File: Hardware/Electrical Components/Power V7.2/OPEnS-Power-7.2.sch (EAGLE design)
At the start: 26 parts, among them U2 DS3231SNT&R, U3 LM2575SX-5.0/NOPB

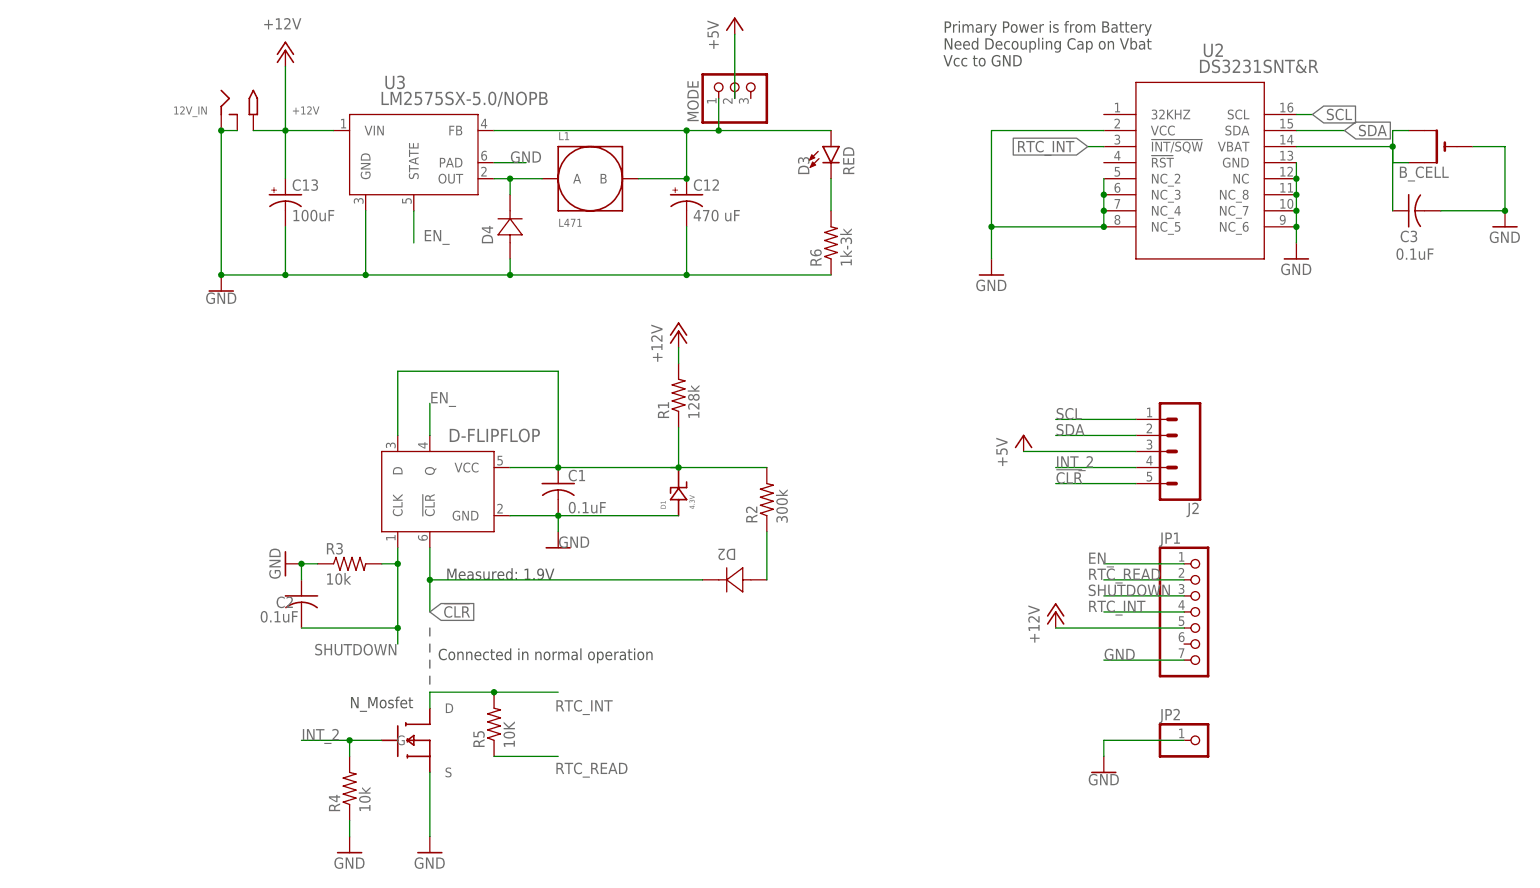
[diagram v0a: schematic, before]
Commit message: Bug fix for Powerboard 7.2V
Changed R5 and R2 value to protect against RTC_READ floating when feather is as sleep.
Added C4 capacitor to further protect against floating RTC_READ.
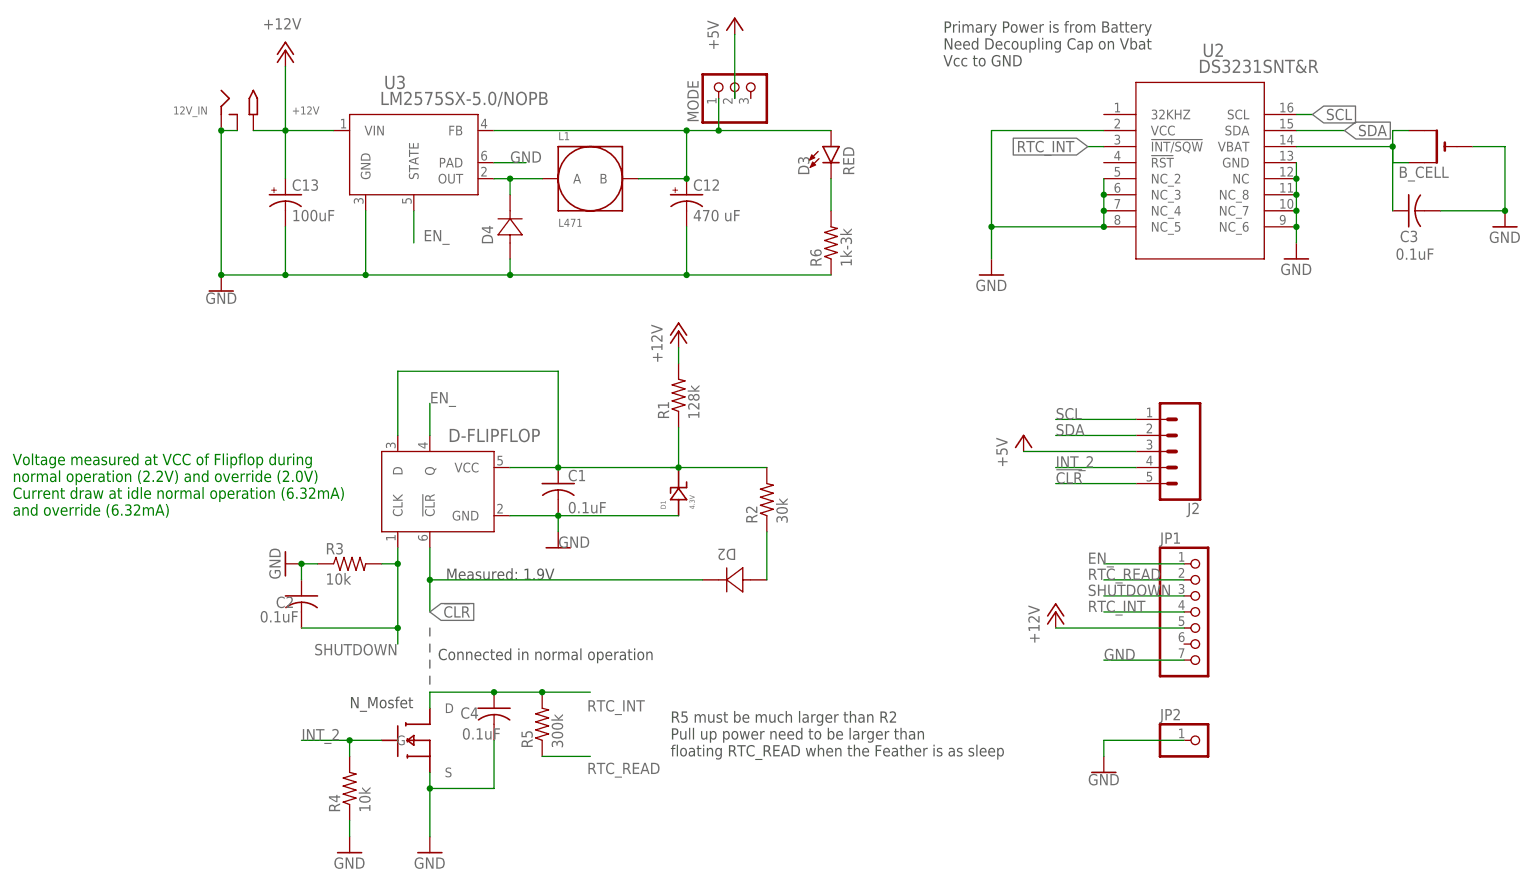
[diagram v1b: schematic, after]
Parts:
- added C4: 0.1uF, adafruit:C-USC1206
- R2: value 300k -> 30k
- R5: value 10K -> 300k
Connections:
- net GND: now also C4.2
- net RTC_INT: now also C4.1
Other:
- note added: "R5 must be much larger than R2 Pull up power need to be larger than floating RTC_READ when the Feather is as sleep"
- note added: "Voltage measured at VCC of Flipflop during normal operation (2.2V) and override (2.0V) Current draw at idle normal operation (6.32mA) and override (6.32mA)"
- moved on the sheet: R5
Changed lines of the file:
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@@
 <part name="D1" library="beach" deviceset="ZENER-DO219" device="" value="4.3V"/>
 <part name="R1" library="adafruit" library_urn="urn:adsk.eagle:library:420" deviceset="R-US_" device="R1206" package3d_urn="urn:adsk.eagle:package:6240569/1" value="128k"/>
-<part name="R2" library="adafruit" library_urn="urn:adsk.eagle:library:420" deviceset="R-US_" device="R1206" package3d_urn="urn:adsk.eagle:package:6240569/1" value="300k"/>
+<part name="R2" library="adafruit" library_urn="urn:adsk.eagle:library:420" deviceset="R-US_" device="R1206" package3d_urn="urn:adsk.eagle:package:6240569/1" value="30k"/>
 <part name="R3" library="adafruit" library_urn="urn:adsk.eagle:library:420" deviceset="R-US_" device="R1206" package3d_urn="urn:adsk.eagle:package:6240569/1" value="10k"/>
 <part name="C1" library="adafruit" library_urn="urn:adsk.eagle:library:420" deviceset="C-US" device="C1206" package3d_urn="urn:adsk.eagle:package:6240335/1" value="0.1uF"/>
@@
 <part name="JP1" library="pinhead" library_urn="urn:adsk.eagle:library:325" deviceset="PINHD-1X7" device="" package3d_urn="urn:adsk.eagle:package:22477/2"/>
 <part name="P+7" library="supply1" library_urn="urn:adsk.eagle:library:371" deviceset="+12V" device=""/>
-<part name="R5" library="adafruit" library_urn="urn:adsk.eagle:library:420" deviceset="R-US_" device="R1206" package3d_urn="urn:adsk.eagle:package:6240569/1" value="10K"/>
+<part name="R5" library="adafruit" library_urn="urn:adsk.eagle:library:420" deviceset="R-US_" device="R1206" package3d_urn="urn:adsk.eagle:package:6240569/1" value="300k"/>
 <part name="U3" library="eDNA" deviceset="LM2575SX-5.0/NOPB" device=""/>
 <part name="D3" library="SparkFun-LED" library_urn="urn:adsk.eagle:library:529" deviceset="LED-RED" device="1206" package3d_urn="urn:adsk.eagle:package:39352/1" value="RED"/>
@@
 <part name="JP2" library="adafruit" library_urn="urn:adsk.eagle:library:420" deviceset="PINHD-1X1" device="" package3d_urn="urn:adsk.eagle:package:6240654/1"/>
 <part name="GND3" library="SparkFun-PowerSymbols" library_urn="urn:adsk.eagle:library:530" deviceset="GND" device=""/>
+<part name="C4" library="adafruit" library_urn="urn:adsk.eagle:library:420" deviceset="C-US" device="C1206" package3d_urn="urn:adsk.eagle:package:6240335/1" value="0.1uF"/>
 </parts>
 <sheets>
@@
 <text x="52.07" y="58.42" size="1.778" layer="97">Connected in normal operation</text>
 <text x="38.1" y="50.8" size="1.778" layer="97">N_Mosfet</text>
+<text x="-15.24" y="81.28" size="1.778" layer="91">Voltage measured at VCC of Flipflop during
+normal operation (2.2V) and override (2.0V)
+Current draw at idle normal operation (6.32mA)
+and override (6.32mA)</text>
+<text x="88.9" y="43.18" size="1.778" layer="97">R5 must be much larger than R2
+Pull up power need to be larger than
+floating RTC_READ when the Feather is as sleep</text>
 </plain>
 <instances>
@@
 <attribute name="VALUE" x="147.32" y="60.96" size="1.778" layer="96" rot="R90"/>
 </instance>
-<instance part="R5" gate="G$1" x="60.96" y="48.26" smashed="yes" rot="R90">
-<attribute name="NAME" x="59.4614" y="44.45" size="1.778" layer="95" rot="R90"/>
-<attribute name="VALUE" x="64.262" y="44.45" size="1.778" layer="96" rot="R90"/>
+<instance part="R5" gate="G$1" x="68.58" y="48.26" smashed="yes" rot="R90">
+<attribute name="NAME" x="67.0814" y="44.45" size="1.778" layer="95" rot="R90"/>
+<attribute name="VALUE" x="71.882" y="44.45" size="1.778" layer="96" rot="R90"/>
 </instance>
 <instance part="U3" gate="A" x="45.72" y="137.16" smashed="yes">
@@
 <instance part="GND3" gate="1" x="157.48" y="40.64" smashed="yes">
 <attribute name="VALUE" x="157.48" y="40.386" size="1.778" layer="96" align="top-center"/>
+</instance>
+<instance part="C4" gate="G$1" x="60.96" y="50.8" smashed="yes">
+<attribute name="NAME" x="55.626" y="49.149" size="1.778" layer="95"/>
+<attribute name="VALUE" x="55.88" y="45.847" size="1.778" layer="96"/>
 </instance>
 </instances>
@@
 </segment>
 <segment>
-<label x="70.612" y="50.292" size="1.778" layer="95"/>
+<label x="75.692" y="50.292" size="1.778" layer="95"/>
 <pinref part="R5" gate="G$1" pin="2"/>
-<wire x1="60.96" y1="53.34" x2="71.12" y2="53.34" width="0.1524" layer="91"/>
+<wire x1="68.58" y1="53.34" x2="76.2" y2="53.34" width="0.1524" layer="91"/>
 <pinref part="MOSFET" gate="G$1" pin="D"/>
 <wire x1="50.8" y1="50.8" x2="50.8" y2="53.34" width="0.1524" layer="91"/>
 <wire x1="50.8" y1="53.34" x2="60.96" y2="53.34" width="0.1524" layer="91"/>
+<junction x="68.58" y="53.34"/>
+<pinref part="C4" gate="G$1" pin="1"/>
+<wire x1="60.96" y1="53.34" x2="68.58" y2="53.34" width="0.1524" layer="91"/>
 <junction x="60.96" y="53.34"/>
 </segment>
@@
 <pinref part="MOSFET" gate="G$1" pin="S"/>
 <pinref part="GND4" gate="1" pin="GND"/>
-<wire x1="50.8" y1="40.64" x2="50.8" y2="30.48" width="0.1524" layer="91"/>
+<wire x1="50.8" y1="40.64" x2="50.8" y2="38.1" width="0.1524" layer="91"/>
+<pinref part="C4" gate="G$1" pin="2"/>
+<wire x1="50.8" y1="38.1" x2="50.8" y2="30.48" width="0.1524" layer="91"/>
+<wire x1="60.96" y1="45.72" x2="60.96" y2="38.1" width="0.1524" layer="91"/>
+<wire x1="60.96" y1="38.1" x2="50.8" y2="38.1" width="0.1524" layer="91"/>
+<junction x="50.8" y="38.1"/>
 </segment>
 <segment>
@@
 <segment>
 <pinref part="R5" gate="G$1" pin="1"/>
-<wire x1="60.96" y1="43.18" x2="71.12" y2="43.18" width="0.1524" layer="91"/>
-<label x="70.612" y="40.386" size="1.778" layer="95"/>
-</segment>
-</net>
+<wire x1="68.58" y1="43.18" x2="76.2" y2="43.18" width="0.1524" layer="91"/>
+<label x="75.692" y="40.386" size="1.778" layer="95"/>
+</segment>
+</net>
